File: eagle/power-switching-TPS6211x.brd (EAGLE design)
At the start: 36 x 27 mm, 17 parts, among them U1 TPS6211X

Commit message: Notes for TPS6211x
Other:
- board text added: "Step-down TPS62111/2 PSAS / OreSat 2019-09-07 v1.0 E.M. - KJ7AOG"
- board text removed: "Step-down TPS6211x PSAS / OreSat 2019-09-07 v1.0 E.M. - KJ7AOG"
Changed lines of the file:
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@@
 <drawing>
 <settings>
-<setting alwaysvectorfont="yes"/>
+<setting alwaysvectorfont="no"/>
 <setting verticaltext="up"/>
 </settings>
@@
 <text x="10.8" y="9.1" size="1" layer="21" font="vector" ratio="15">VOUT</text>
 <text x="1.3" y="12.3" size="0.8" layer="21" font="vector" ratio="15" rot="R90">SYNC</text>
-<text x="28.9" y="11.2" size="1.5" layer="22" font="vector" ratio="15" rot="MR0">Step-down TPS6211x
+<text x="28.9" y="11.2" size="1.5" layer="22" font="vector" ratio="15" rot="MR0">Step-down TPS62111/2
 PSAS / OreSat
 2019-09-07  v1.0

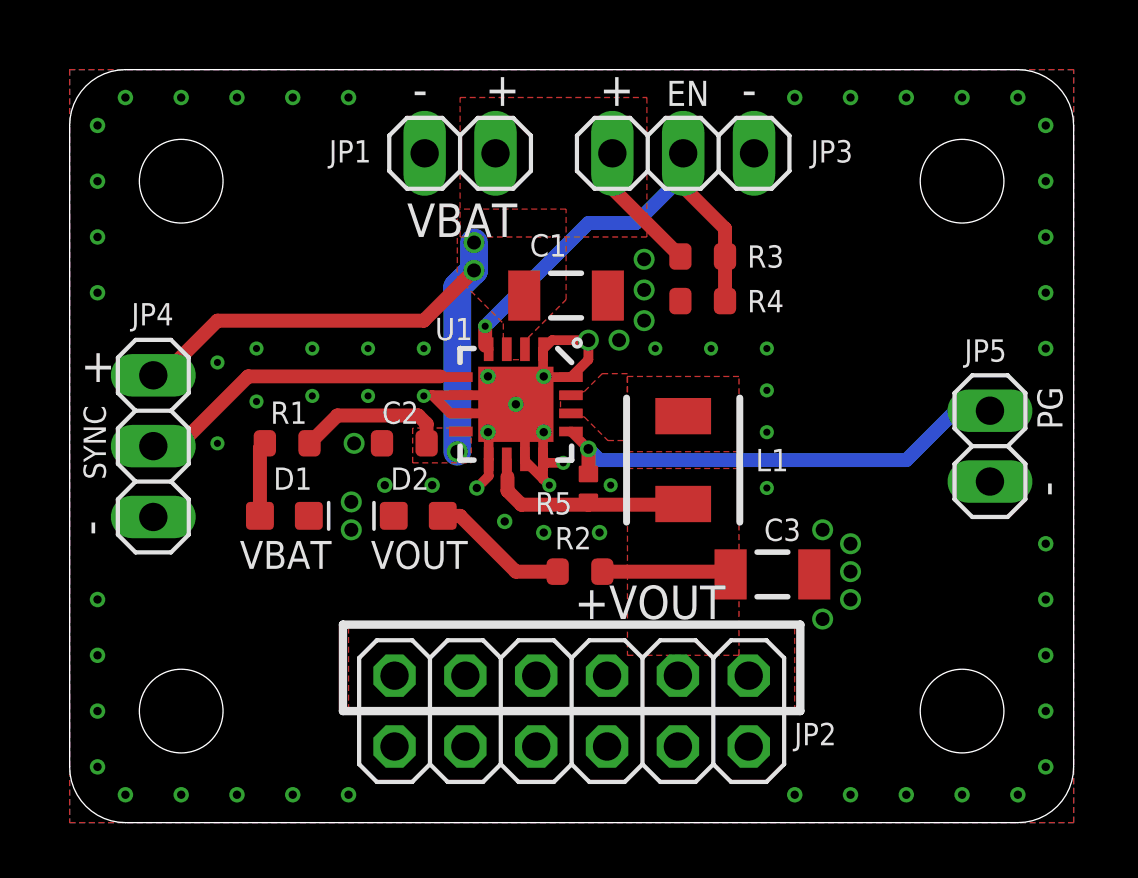
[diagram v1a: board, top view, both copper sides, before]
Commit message: Add adj and power bad LED for TPS6211x
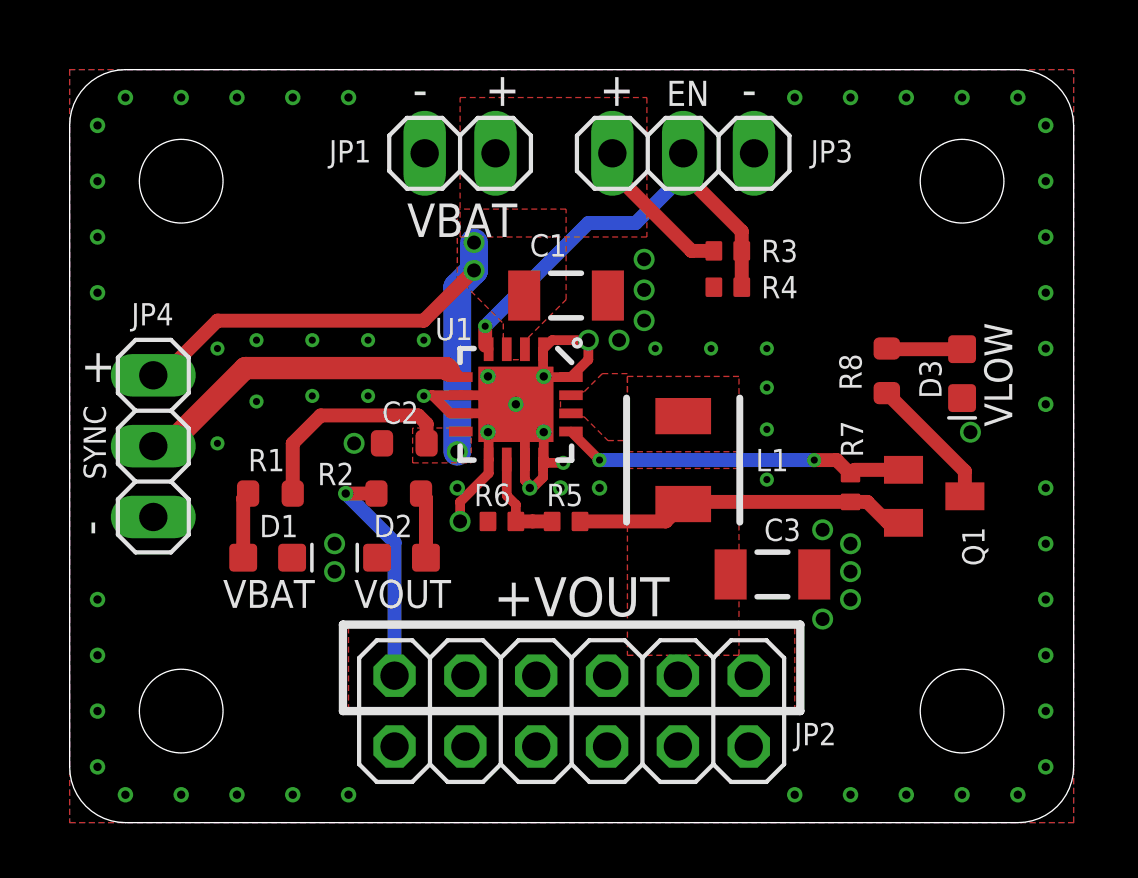
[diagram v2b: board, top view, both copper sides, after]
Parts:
- removed JP5: (no value), pinhead:1X02
- added D3: RED, SparkFun-LED:LED-0603
- added Q1: PMOS, transistor-small-signal:SOT23
- added R6: NP, oresat-rcl:.0402-B-NOSILK
- added R7: 100k, oresat-rcl:.0402-B-NOSILK
- added R8: 2.7k, oresat-rcl:.0603-B-NOSILK
- R3, R4: device oresat-rcl:.0603-B-NOSILK -> oresat-rcl:.0402-B-NOSILK
- R5: value 1M -> NP
- moved R2 7.08 mm to (11.8, 11.8), turned to 180 degrees
- moved R1 1.90 mm to (7.20, 11.8)
- moved D1 1.62 mm to (7.10, 9.50)
- moved D2 1.62 mm to (11.9, 9.50)
- moved R5 1.44 mm to (17.8, 10.8), turned to 0 degrees
- moved R4 1.03 mm to (23.6, 19.2)
- moved R3 0.92 mm to (23.6, 20.5)
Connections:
- new net +VOUT1: Q1.3, R8.2
- new net FB: R5.1, R6.2, U1.10
- new net N$3: D3.A, R8.1
- net +VOUT: now also Q1.2, R7.2; no longer U1.10
- net GND: now also D3.C, R6.1; no longer JP5.1
- net PG: now also Q1.1, R7.1; no longer JP5.2, R5.1
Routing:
- net +VOUT: track 12.4 -> 20.7 mm, vias 0 -> 1
- net +VOUT1: track 0.00 -> 4.86 mm
- net PG: track 17.1 -> 12.6 mm, vias 1 -> 2
- net FB: track 0.00 -> 3.66 mm
- net +VIN: track 31.0 -> 34.2 mm
- net N$3: track 0.00 -> 2.71 mm
- net N$271: track 4.95 -> 2.37 mm
- net GND: track 19.9 -> 21.7 mm
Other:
- board text added: "Step-down TPS6211x fix/adj PSAS / OreSat 2019-09-08 v1.0 E.M. - KJ7AOG"
- board text added: "VLOW"
- board text removed: "PG"
- board text removed: "Step-down TPS62111/2 PSAS / OreSat 2019-09-07 v1.0 E.M. - KJ7AOG"

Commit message: Minor fix TPS6211x
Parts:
- R5: value NP -> 0
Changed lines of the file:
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@@
 <drawing>
 <settings>
-<setting alwaysvectorfont="yes"/>
+<setting alwaysvectorfont="no"/>
 <setting verticaltext="up"/>
 </settings>
@@
 <attribute name="NAME" x="13.1" y="17.3" size="0.8" layer="25" font="vector" ratio="20"/>
 </element>
-<element name="R5" library="oresat-rcl" package=".0402-B-NOSILK" value="NP" x="17.8" y="10.8" smashed="yes">
+<element name="R5" library="oresat-rcl" package=".0402-B-NOSILK" value="0" x="17.8" y="10.8" smashed="yes">
 <attribute name="NAME" x="17.1" y="11.35" size="0.8" layer="25" font="vector" ratio="15"/>
 <attribute name="NAME" x="17.8" y="10.8" size="0.2" layer="33" ratio="15" align="center"/>

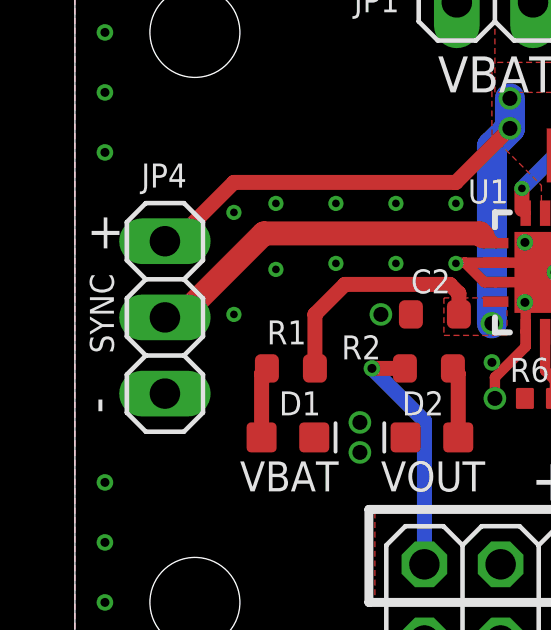
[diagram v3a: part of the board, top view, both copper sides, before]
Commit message: Power boards add gnd for mounts
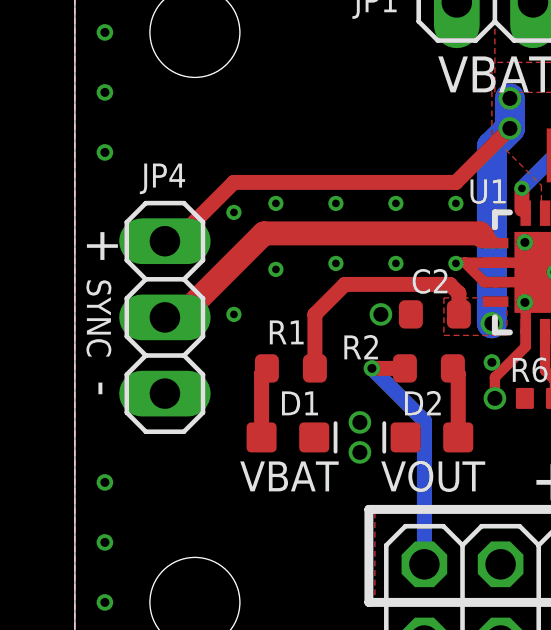
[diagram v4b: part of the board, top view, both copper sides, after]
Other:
- board text added: "Step-down TPS6211x fix/adj PSAS / OreSat 2019-09-12 v1.0 E.M. - KJ7AOG"
- board text removed: "Step-down TPS6211x fix/adj PSAS / OreSat 2019-09-08 v1.0 E.M. - KJ7AOG"
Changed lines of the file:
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@@
 <drawing>
 <settings>
-<setting alwaysvectorfont="no"/>
+<setting alwaysvectorfont="yes"/>
 <setting verticaltext="up"/>
 </settings>
@@
 <layer number="20" name="Dimension" color="24" fill="1" visible="yes" active="yes"/>
 <layer number="21" name="tPlace" color="7" fill="1" visible="yes" active="yes"/>
-<layer number="22" name="bPlace" color="7" fill="1" visible="no" active="yes"/>
+<layer number="22" name="bPlace" color="7" fill="1" visible="yes" active="yes"/>
 <layer number="23" name="tOrigins" color="15" fill="1" visible="yes" active="yes"/>
 <layer number="24" name="bOrigins" color="15" fill="1" visible="yes" active="yes"/>
@@
 <layer number="27" name="tValues" color="7" fill="1" visible="yes" active="yes"/>
 <layer number="28" name="bValues" color="7" fill="1" visible="yes" active="yes"/>
-<layer number="29" name="tStop" color="7" fill="3" visible="no" active="yes"/>
-<layer number="30" name="bStop" color="7" fill="6" visible="no" active="yes"/>
+<layer number="29" name="tStop" color="7" fill="3" visible="yes" active="yes"/>
+<layer number="30" name="bStop" color="7" fill="6" visible="yes" active="yes"/>
 <layer number="31" name="tCream" color="7" fill="4" visible="no" active="yes"/>
 <layer number="32" name="bCream" color="7" fill="5" visible="no" active="yes"/>
@@
 <text x="14.9" y="25.7" size="1.2" layer="21" font="vector" ratio="15">+</text>
 <text x="33.8" y="14.2" size="1" layer="21" font="vector" ratio="15" rot="R90">VLOW</text>
-<text x="0.4" y="15.8" size="1.2" layer="21" font="vector" ratio="15">+</text>
-<text x="1.3" y="10.3" size="1.2" layer="21" font="vector" ratio="15" rot="R90">-</text>
+<text x="0.4" y="16.5" size="1.2" layer="21" font="vector" ratio="15" rot="SR270">+</text>
+<text x="0.4" y="11.4" size="1.2" layer="21" font="vector" ratio="15" rot="SR270">-</text>
 <text x="12.3" y="25.7" size="1.2" layer="21" font="vector" ratio="15">-</text>
 <text x="24.1" y="25.7" size="1.2" layer="21" font="vector" ratio="15">-</text>
 <text x="5.5" y="7.7" size="1" layer="21" font="vector" ratio="15">VBAT</text>
 <text x="10.2" y="7.7" size="1" layer="21" font="vector" ratio="15">VOUT</text>
-<text x="1.3" y="12.3" size="0.8" layer="21" font="vector" ratio="15" rot="R90">SYNC</text>
-<text x="33.4" y="11.2" size="1.5" layer="22" font="vector" ratio="15" rot="MR0">Step-down TPS6211x fix/adj
+<text x="0.4" y="14.8" size="0.8" layer="21" font="vector" ratio="15" rot="SR270">SYNC</text>
+<text x="33.4" y="10.8" size="1.5" layer="22" font="vector" ratio="15" rot="MR0">Step-down TPS6211x fix/adj
 PSAS / OreSat
-2019-09-08  v1.0
+2019-09-12  v1.0
 E.M. - KJ7AOG</text>
+<circle x="4" y="23" radius="2" width="3" layer="29"/>
+<circle x="32" y="23" radius="2" width="3" layer="29"/>
+<circle x="4" y="4" radius="2" width="3" layer="29"/>
+<circle x="32" y="4" radius="2" width="3" layer="29"/>
+<circle x="32" y="23" radius="2" width="3" layer="30"/>
+<circle x="32" y="4" radius="2" width="3" layer="30"/>
+<circle x="4" y="4" radius="2" width="3" layer="30"/>
+<circle x="4" y="23" radius="2" width="3" layer="30"/>
 </plain>
 <attributes>

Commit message: TPS6211x - update values
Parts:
- C1: value 10u -> 22u
- R7: value 100k -> 47k
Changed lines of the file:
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@@
 <drawing>
 <settings>
-<setting alwaysvectorfont="yes"/>
+<setting alwaysvectorfont="no"/>
 <setting verticaltext="up"/>
 </settings>
@@
 </autorouter>
 <elements>
-<element name="C1" library="oresat-rcl" package="1206-B" value="10u" x="17.8" y="18.9" smashed="yes">
+<element name="C1" library="oresat-rcl" package="1206-B" value="22u" x="17.8" y="18.9" smashed="yes">
 <attribute name="NAME" x="16.5" y="20.3" size="0.8" layer="25" font="vector" ratio="15"/>
 <attribute name="NAME" x="17.8" y="18.9" size="0.4" layer="33" ratio="15" align="center"/>
@@
 <attribute name="NAME" x="23.6" y="20.5" size="0.3" layer="33" ratio="15" rot="R180" align="center"/>
 </element>
-<element name="R7" library="oresat-rcl" package=".0402-B-NOSILK" value="100k" x="28" y="12" smashed="yes" rot="R270">
+<element name="R7" library="oresat-rcl" package=".0402-B-NOSILK" value="47k" x="28" y="12" smashed="yes" rot="R270">
 <attribute name="NAME" x="28.45" y="13.1" size="0.8" layer="25" font="vector" ratio="15" rot="R90"/>
 <attribute name="NAME" x="28" y="12" size="0.2" layer="33" ratio="15" rot="R270" align="center"/>
